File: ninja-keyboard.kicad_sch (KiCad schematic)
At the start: 265 parts, among them J1 Conn_01x05_Pin, J3 USB_C_Receptacle_USB2.0_14P, J4 Conn_01x02, Q1 SS8050, Q2 AO3401A, SW1 backquote, SW10 num9, SW11 num0, SW12 -, SW13 =, SW14 backsapce, SW15 tab, SW16 q, SW17 w, SW18 e, SW19 r, SW2 num1, SW20 t, SW21 y, SW22 u, SW23 i, SW24 o, SW25 p, SW26 [, SW27 ], SW28 \, SW29 cap, SW3 num2, SW30 a, SW31 s, SW32 d, SW33 f, SW34 h, SW35 g, SW36 j, SW37 k, SW38 l, SW39 semicolon, SW4 num3, SW40 apostrophe, SW41 enter, SW42 lshift, SW43 z, SW44 x, SW45 c, SW46 v, SW47 b, SW48 n, SW49 m, SW5 num4, SW50 comma, SW51 period, SW52 /, SW53 rshift, SW54 lctrl, SW55 win, SW56 lalt, SW57 space, SW58 ralt, SW59 win, SW6 num5, SW60 menu, SW61 rctrl, SW62 RotaryEncoder, SW63 SW_SPDT, SW7 num6, SW8 num7, SW9 num8, U1 ESP32-S3-WROOM-1, U2 TP4056-42-ESOP8

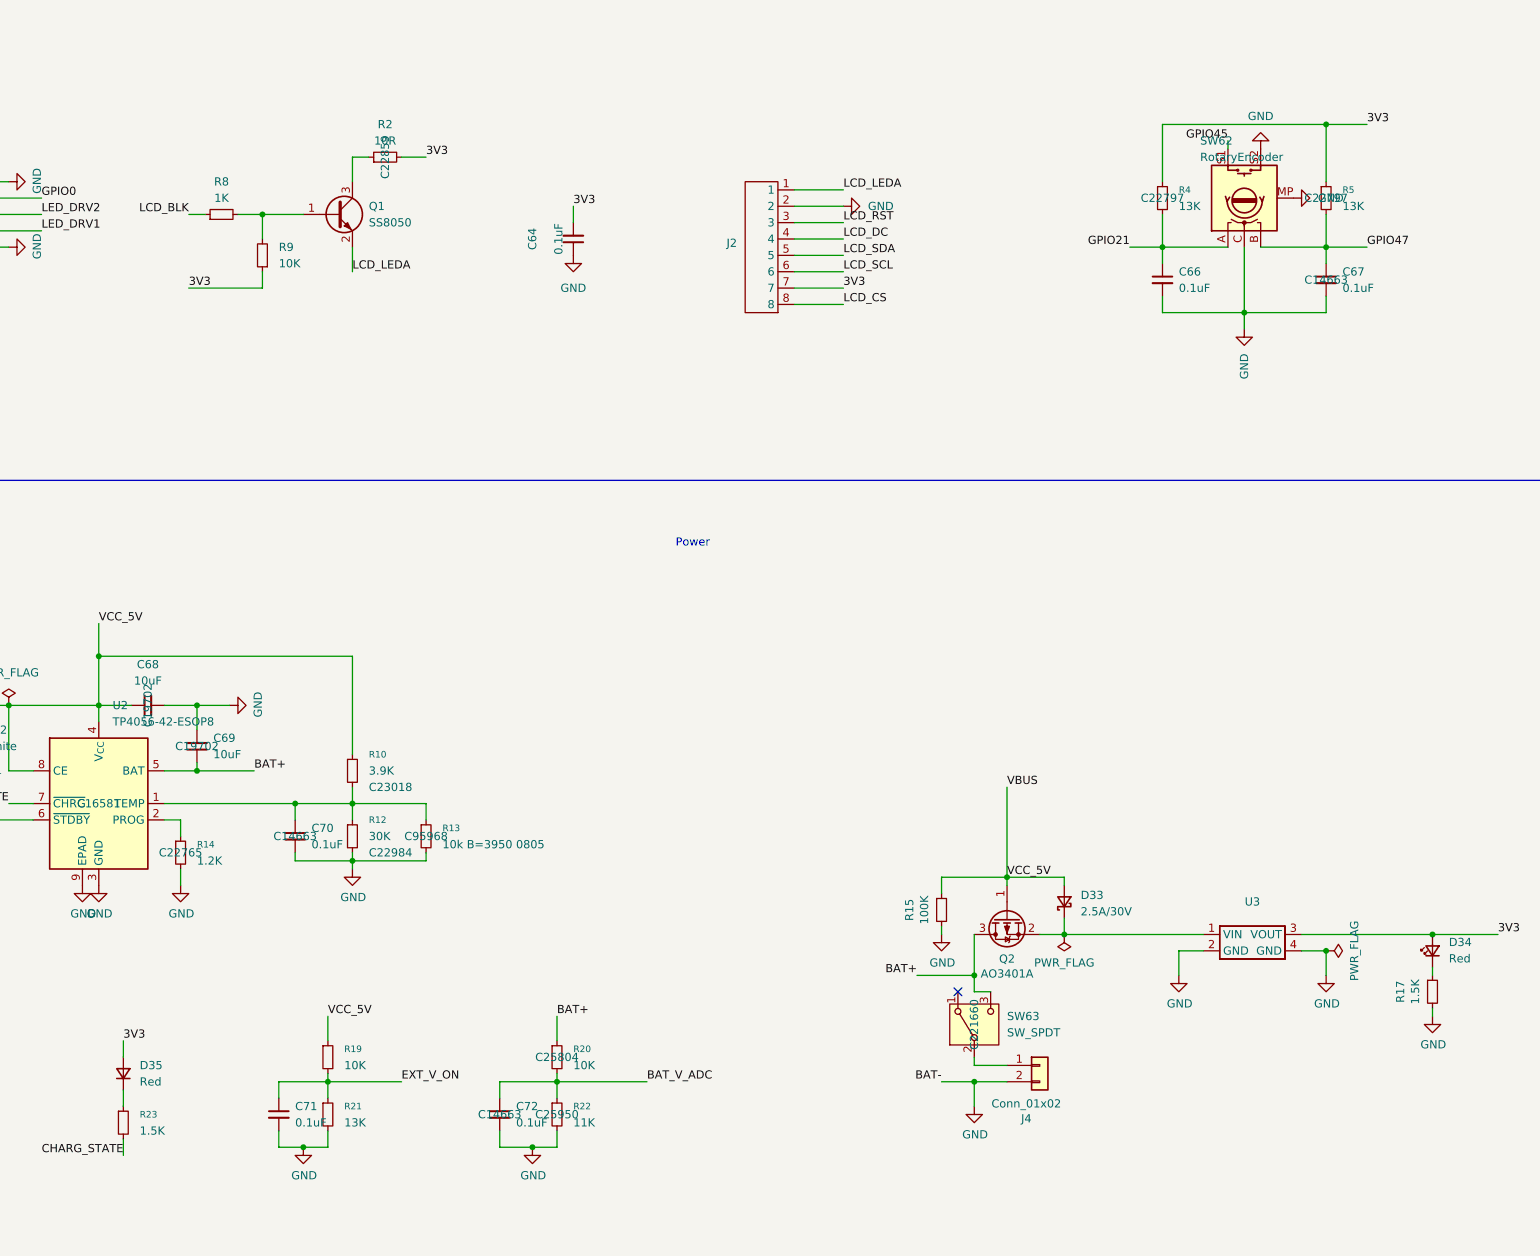
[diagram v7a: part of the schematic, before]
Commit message: remove parts belong to the lcd sub board
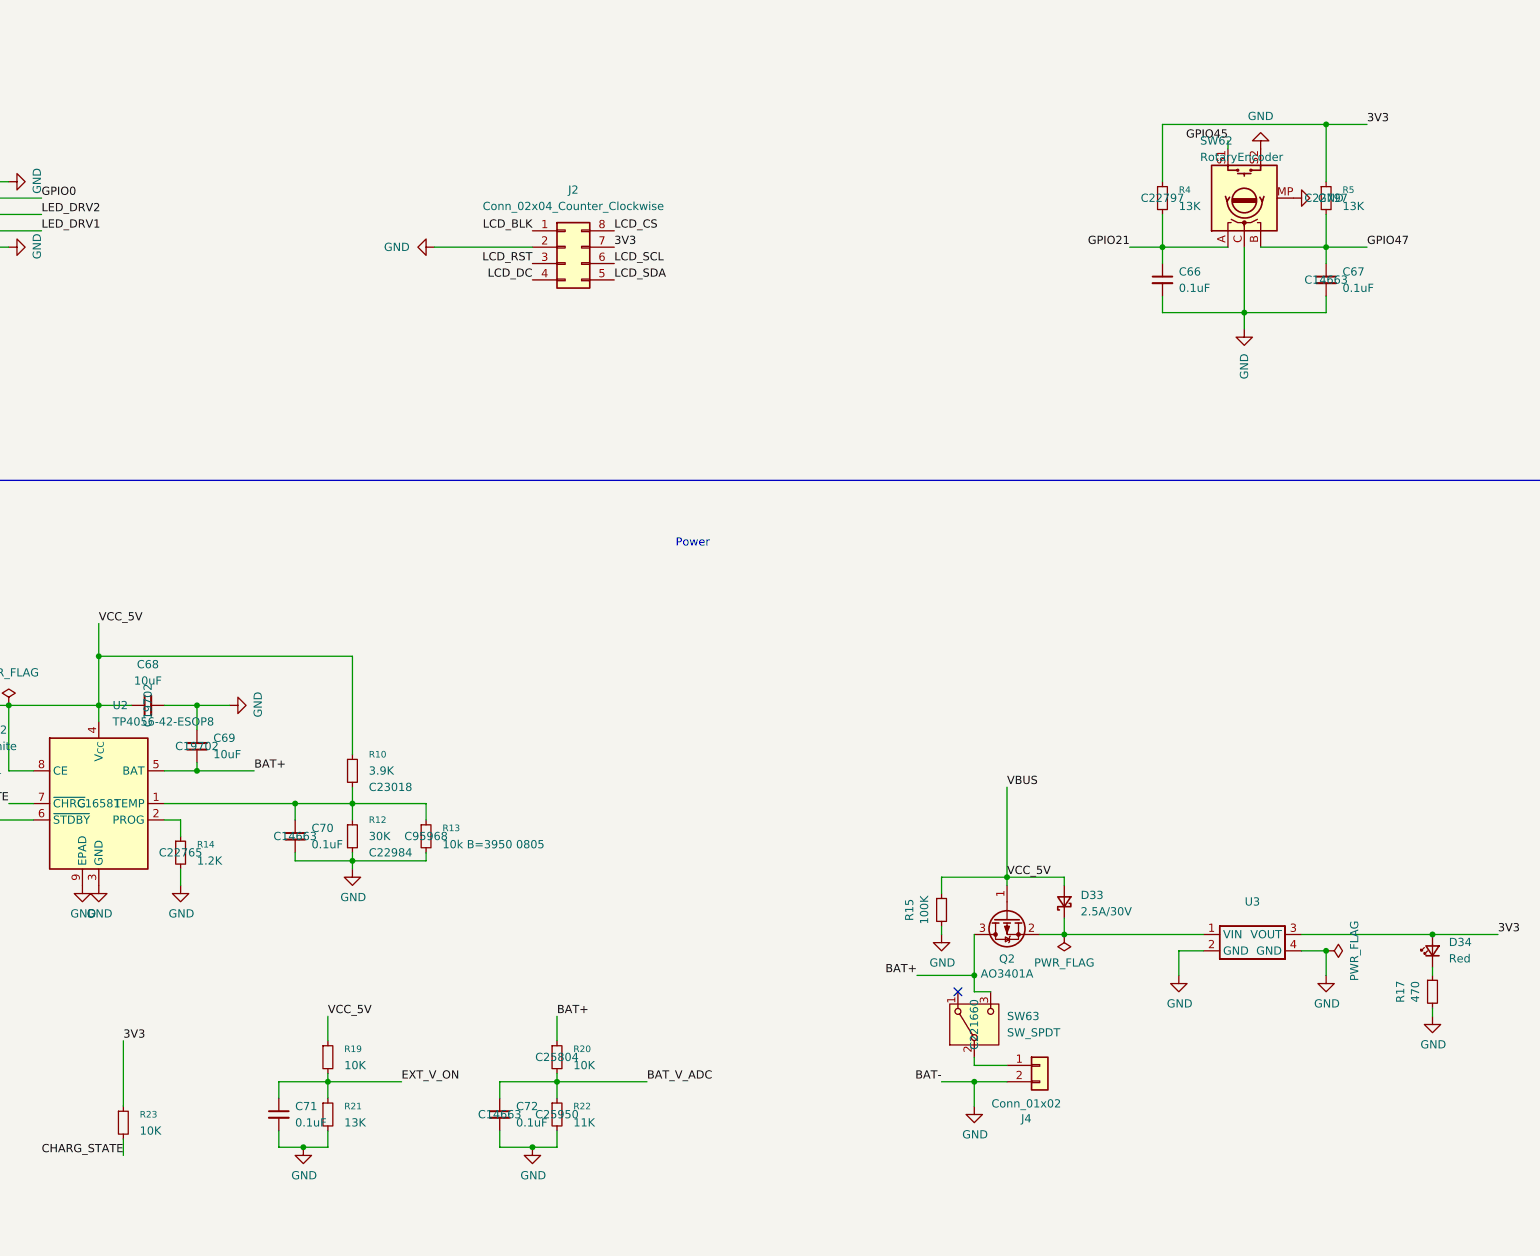
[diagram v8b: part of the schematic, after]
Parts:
- removed C64: 0.1uF, Capacitor_SMD:C_0603_1608Metric, symbol Device:C_Small
- removed D35: Red, LED_SMD:LED_0603_1608Metric, symbol Device:D_Small
- removed J2: ~, user_added:taobao 1x8 P0.5mm drawer bottom-side, symbol user_created:FPC_Connector_bottom_8_pin
- removed Q1: SS8050, Package_TO_SOT_SMD:SOT-23, symbol Transistor_BJT:SS8050
- removed R2: 10R, Resistor_SMD:R_0603_1608Metric, symbol Device:R_Small
- removed R8: 1K, Resistor_SMD:R_0603_1608Metric, symbol Device:R_Small
- removed R9: 10K, Resistor_SMD:R_0603_1608Metric, symbol Device:R_Small
- added J2: Conn_02x04_Counter_Clockwise, Connector_PinSocket_2.54mm:PinSocket_2x04_P2.54mm_Vertical, symbol Connector_Generic:Conn_02x04_Counter_Clockwise
- R17: value 1.5K -> 470; LCSC Part # C22843 -> C23179
- R23: value 1.5K -> 10K; LCSC Part # C22843 -> C25804
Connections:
- net 3V3: now also R23.1, J2.7 (Pin_7)
- net GND: now also J2.2 (Pin_2)
- net LCD_BLK: now also J2.1 (Pin_1)
- net LCD_CS: now also J2.8 (Pin_8)
- net LCD_DC: now also J2.4 (Pin_4)
- net LCD_RST: now also J2.3 (Pin_3)
- net LCD_SCL: now also J2.6 (Pin_6)
- net LCD_SDA: now also J2.5 (Pin_5)
